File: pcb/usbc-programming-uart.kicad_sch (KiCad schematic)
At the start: 27 parts, among them J4 HC-TYPE-C-16P-01A, Q6 MMBT2222A, Q7 MMBT2222A, SW2 RST, SW3 BOOT, U11 CH334R, U12 CH340C, U13 LM1117IMPX-3.3, Y1 12MHz

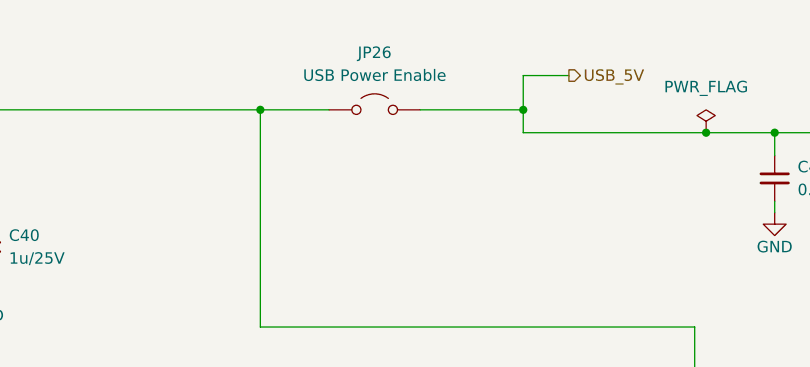
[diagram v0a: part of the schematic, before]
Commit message: audio path
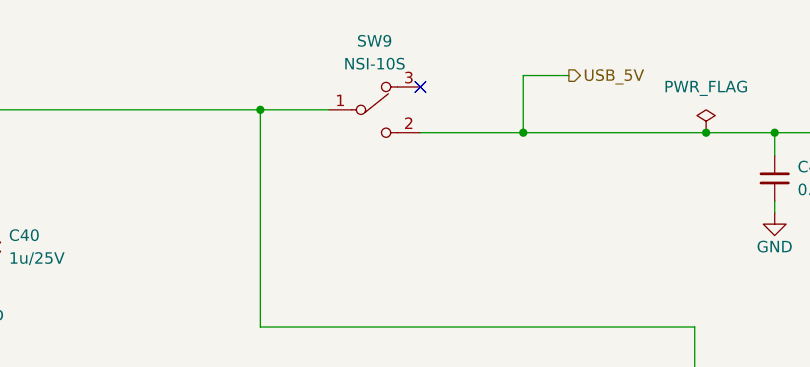
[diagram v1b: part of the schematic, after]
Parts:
- removed JP26: USB Power Enable, TestPoint:TestPoint_2Pads_Pitch2.54mm_Drill0.8mm, symbol Jumper:Jumper_2_Open
- added SW9: NSI-10S, kicad_gx_library:SW-SMD_NSI-10S, symbol kicad_gx_library:NSI-10S
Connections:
- net USB_5V: now also SW9.2
- net at C40.1, C42.1, F3.2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: now also SW9.1
- no-connect marks 10 -> 11
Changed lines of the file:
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@@
 	)
 	(junction
+		(at 195.58 25.4)
+		(diameter 0)
+		(color 0 0 0 0)
+	)
+	(junction
 		(at 100.33 180.34)
 		(diameter 0)
@@
 	)
 	(junction
-		(at 120.65 180.34)
+		(at 166.37 22.86)
 		(diameter 0)
 		(color 0 0 0 0)
 	)
 	(junction
-		(at 247.65 25.4)
+		(at 120.65 180.34)
 		(diameter 0)
 		(color 0 0 0 0)
 	)
 	(junction
-		(at 78.74 132.08)
+		(at 247.65 25.4)
 		(diameter 0)
 		(color 0 0 0 0)
 	)
 	(junction
-		(at 166.37 22.86)
+		(at 78.74 132.08)
 		(diameter 0)
 		(color 0 0 0 0)
@@
 	)
 	(junction
-		(at 195.58 22.86)
-		(diameter 0)
-		(color 0 0 0 0)
-	)
-	(junction
 		(at 214.63 121.92)
 		(diameter 0)
@@
 	)
 	(no_connect
+		(at 184.15 20.32)
+	)
+	(no_connect
 		(at 198.12 139.7)
 	)
@@
 	(wire
 		(pts
+			(xy 184.15 25.4) (xy 195.58 25.4)
+		)
+		(stroke
+			(width 0)
+			(type default)
+		)
+	)
+	(wire
+		(pts
 			(xy 50.8 52.07) (xy 50.8 49.53)
 		)
@@
 	(wire
 		(pts
-			(xy 195.58 19.05) (xy 195.58 22.86)
+			(xy 195.58 19.05) (xy 195.58 25.4)
 		)
 		(stroke
@@
 	(wire
 		(pts
-			(xy 184.15 22.86) (xy 195.58 22.86)
-		)
-		(stroke
-			(width 0)
-			(type default)
-		)
-	)
-	(wire
-		(pts
 			(xy 201.93 142.24) (xy 198.12 142.24)
 		)
@@
 	(wire
 		(pts
-			(xy 166.37 22.86) (xy 173.99 22.86)
-		)
-		(stroke
-			(width 0)
-			(type default)
-		)
-	)
-	(wire
-		(pts
 			(xy 46.99 57.15) (xy 50.8 57.15)
 		)
@@
 	(wire
 		(pts
+			(xy 166.37 22.86) (xy 173.99 22.86)
+		)
+		(stroke
+			(width 0)
+			(type default)
+		)
+	)
+	(wire
+		(pts
 			(xy 120.65 180.34) (xy 119.38 180.34)
 		)
@@
 	(wire
 		(pts
-			(xy 195.58 25.4) (xy 195.58 22.86)
-		)
-		(stroke
-			(width 0)
-			(type default)
-		)
-	)
-	(wire
-		(pts
 			(xy 87.63 72.39) (xy 91.44 72.39)
 		)
@@
 	)
 	(symbol
-		(lib_id "Jumper:Jumper_2_Open")
-		(at 179.07 22.86 0)
-		(unit 1)
-		(body_style 1)
-		(exclude_from_sim no)
-		(in_bom yes)
-		(on_board yes)
-		(in_pos_files yes)
-		(dnp no)
-		(fields_autoplaced yes)
-		(property "Reference" "JP26"
-			(at 179.07 16.51 0)
-			(show_name no)
-			(do_not_autoplace no)
-			(effects
-				(font
-					(size 1.27 1.27)
-				)
-			)
-		)
-		(property "Value" "USB Power Enable"
-			(at 179.07 19.05 0)
-			(show_name no)
-			(do_not_autoplace no)
-			(effects
-				(font
-					(size 1.27 1.27)
-				)
-			)
-		)
-		(property "Footprint" "TestPoint:TestPoint_2Pads_Pitch2.54mm_Drill0.8mm"
-			(at 179.07 22.86 0)
-			(hide yes)
-			(show_name no)
-			(do_not_autoplace no)
-			(effects
-				(font
-					(size 1.27 1.27)
-				)
-			)
-		)
-		(property "Datasheet" ""
-			(at 179.07 22.86 0)
-			(hide yes)
-			(show_name no)
-			(do_not_autoplace no)
-			(effects
-				(font
-					(size 1.27 1.27)
-				)
-			)
-		)
-		(property "Description" "Jumper, 2-pole, open"
-			(at 179.07 22.86 0)
-			(hide yes)
-			(show_name no)
-			(do_not_autoplace no)
-			(effects
-				(font
-					(size 1.27 1.27)
-				)
-			)
-		)
-		(property "Field10" ""
-			(at 179.07 22.86 0)
-			(hide yes)
-			(show_name no)
-			(do_not_autoplace no)
-			(effects
-				(font
-					(size 1.27 1.27)
-				)
-			)
-		)
-		(pin "2"
-		)
-		(pin "1"
-		)
-		(instances
-			(project "foxhunt1"
-				(path "/8399ba4b-9428-480d-8b65-76cf154b97a5/97991d87-aeba-471b-8b55-fc9d012290ca"
-					(reference "JP26")
-					(unit 1)
-				)
-			)
-		)
-	)
-	(symbol
 		(lib_id "PCM_SparkFun-PowerSymbol:GND")
 		(at 247.65 34.29 0)
@@
 					(unit 1)
 				)
+			)
+		)
+	)
+	(symbol
+		(lib_id "kicad_gx_library:NSI-10S")
+		(at 179.07 24.13 90)
+		(unit 1)
+		(body_style 1)
+		(exclude_from_sim no)
+		(in_bom yes)
+		(on_board yes)
+		(in_pos_files yes)
+		(dnp no)
+		(fields_autoplaced yes)
+		(property "Reference" "SW9"
+			(at 179.07 15.24 90)
+			(show_name no)
+			(do_not_autoplace no)
+			(effects
+				(font
+					(size 1.27 1.27)
+				)
+			)
+		)
+		(property "Value" "NSI-10S"
+			(at 179.07 17.78 90)
+			(show_name no)
+			(do_not_autoplace no)
+			(effects
+				(font
+					(size 1.27 1.27)
+				)
+			)
+		)
+		(property "Footprint" "kicad_gx_library:SW-SMD_NSI-10S"
+			(at 191.77 24.13 0)
+			(hide yes)
+			(show_name no)
+			(do_not_autoplace no)
+			(effects
+				(font
+					(size 1.27 1.27)
+				)
+			)
+		)
+		(property "Datasheet" "https://www.lcsc.com/datasheet/C515802.pdf"
+			(at 194.31 24.13 0)
+			(hide yes)
+			(show_name no)
+			(do_not_autoplace no)
+			(effects
+				(font
+					(size 1.27 1.27)
+				)
+			)
+		)
+		(property "Description" ""
+			(at 179.07 24.13 0)
+			(hide yes)
+			(show_name no)
+			(do_not_autoplace no)
+			(effects
+				(font
+					(size 1.27 1.27)
+				)
+			)
+		)
+		(property "Manufacturer" "SUNGMUN(韩国星炆电子)"
+			(at 196.85 24.13 0)
+			(hide yes)
+			(show_name no)
+			(do_not_autoplace no)
+			(effects
+				(font
+					(size 1.27 1.27)
+				)
+			)
+		)
+		(property "MPN" "NSI-10S"
+			(at 199.39 24.13 0)
+			(hide yes)
+			(show_name no)
+			(do_not_autoplace no)
+			(effects
+				(font
+					(size 1.27 1.27)
+				)
+			)
+		)
+		(property "LCSC Part" "C515802"
+			(at 201.93 24.13 0)
+			(hide yes)
+			(show_name no)
+			(do_not_autoplace no)
+			(effects
+				(font
+					(size 1.27 1.27)
+				)
+			)
+		)
+		(property "Source" "easyeda2kicad"
+			(at 207.01 24.13 0)
+			(hide yes)
+			(show_name no)
+			(do_not_autoplace no)
+			(effects
+				(font
+					(size 1.27 1.27)
+				)
+			)
+		)
+		(property "Imported" "2026-09-23"
+			(at 209.55 24.13 0)
+			(hide yes)
+			(show_name no)
+			(do_not_autoplace no)
+			(effects
+				(font
+					(size 1.27 1.27)
+				)
+			)
+		)
+		(pin "2"
+		)
+		(pin "1"
+		)
+		(pin "3"
+		)
+		(instances
+			(project "foxhunt1"
+				(path "/8399ba4b-9428-480d-8b65-76cf154b97a5/97991d87-aeba-471b-8b55-fc9d012290ca"
+					(reference "SW9")
+					(unit 1)
+				)

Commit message: annotations
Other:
- note added: "BOOT AND RESET - Buttons & ESPTOOL DTR/RTS"
- note added: "USB HUB"
- note added: "USB POWER w/ SWITCH"
- note added: "USB UART"
- moved on the sheet: C43, C44, C45, SW9, U13

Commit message: changes on pcb
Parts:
- removed Y1: 12MHz, Crystal:Crystal_SMD_2520-4Pin_2.5x2.0mm, symbol PCM_SparkFun-Clock:Crystal
- added X1: 12MHz 10pF, kicad_gx_library:CRYSTAL-SMD_4P-L2.5-W2.0-BL, symbol kicad_gx_library:TXM12M0004252DBCEO00T
- U13: footprint Package_TO_SOT_SMD:SOT-223 -> Package_TO_SOT_SMD:SOT-223-3_TabPin2
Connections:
- net USB_5V: now also F3.1, J4.A4 (VBUS), J4.A9 (VBUS), J4.B4 (VBUS), J4.B9 (VBUS); no longer C43.1, SW9.2, U13.3 (VI)
- net USB_5V_Fused: now reaches C40.1, C42.1, F3.2, SW9.1, U11.12 (V5), U12.16 (VCC)
- net at U11.16 (XI): now also X1.1
- net at U11.15 (XO): now also X1.3
- new net USB_5V_SW: C43.1, SW9.2, U13.3 (VI)
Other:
- moved on the sheet: F3
